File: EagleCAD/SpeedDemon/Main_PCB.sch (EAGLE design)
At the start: 71 parts, among them Q1 DMC2700, U3 LM3676, U4 STM32F072-LQFP48, X1 32.768kHz

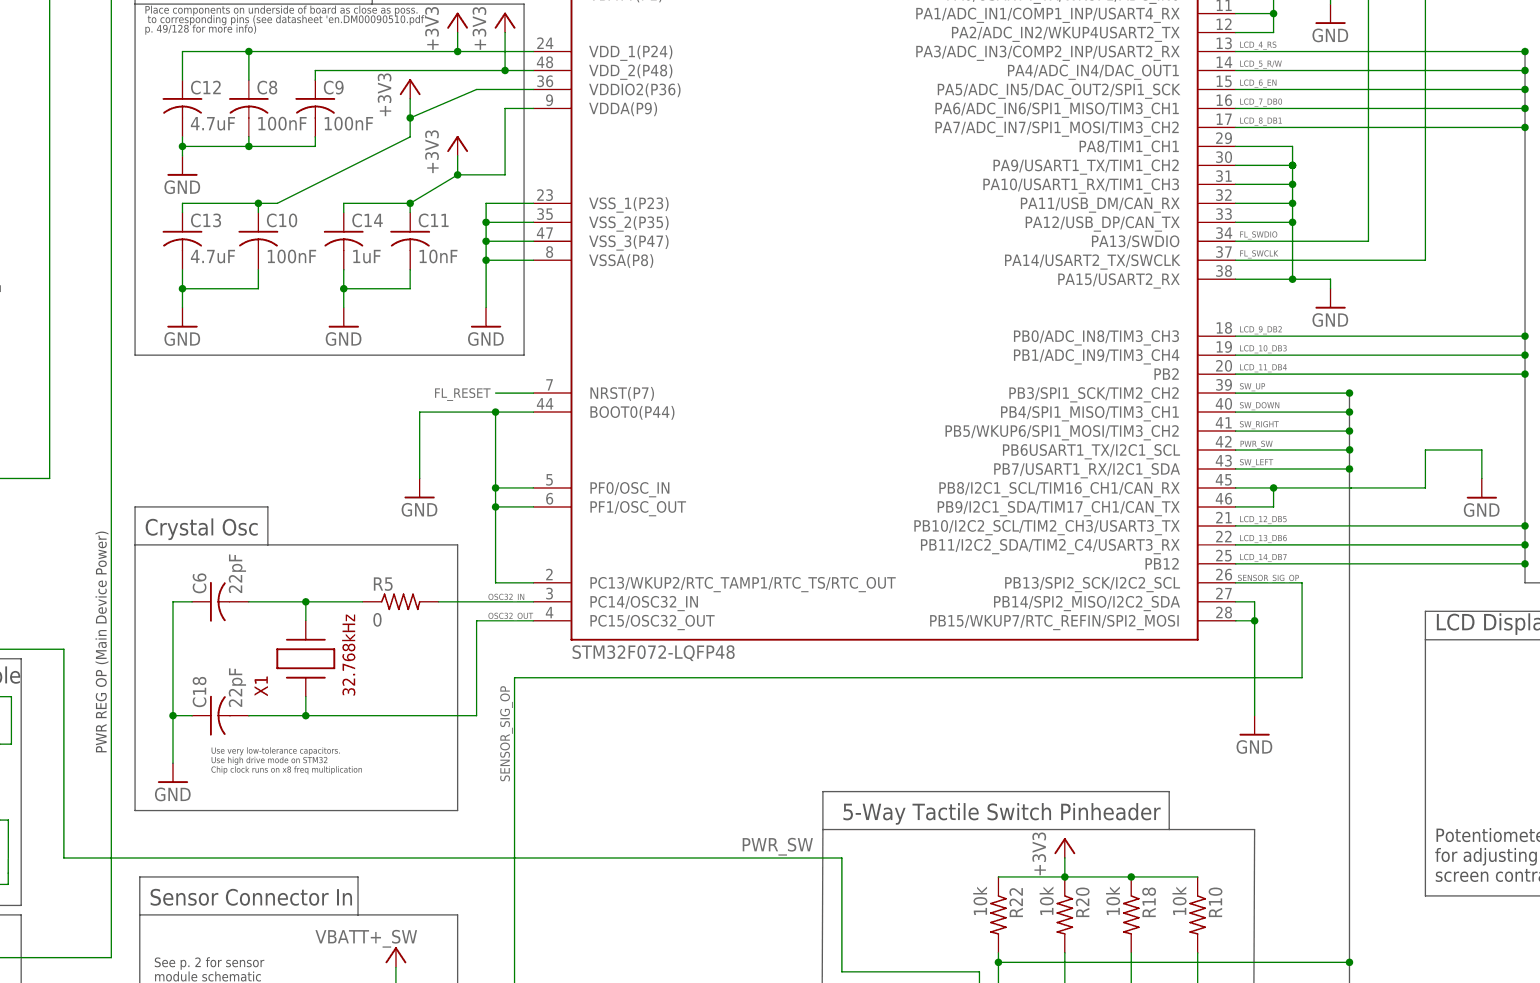
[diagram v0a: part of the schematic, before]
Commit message: added 8MHz oscillator citcuit to layout and schematic
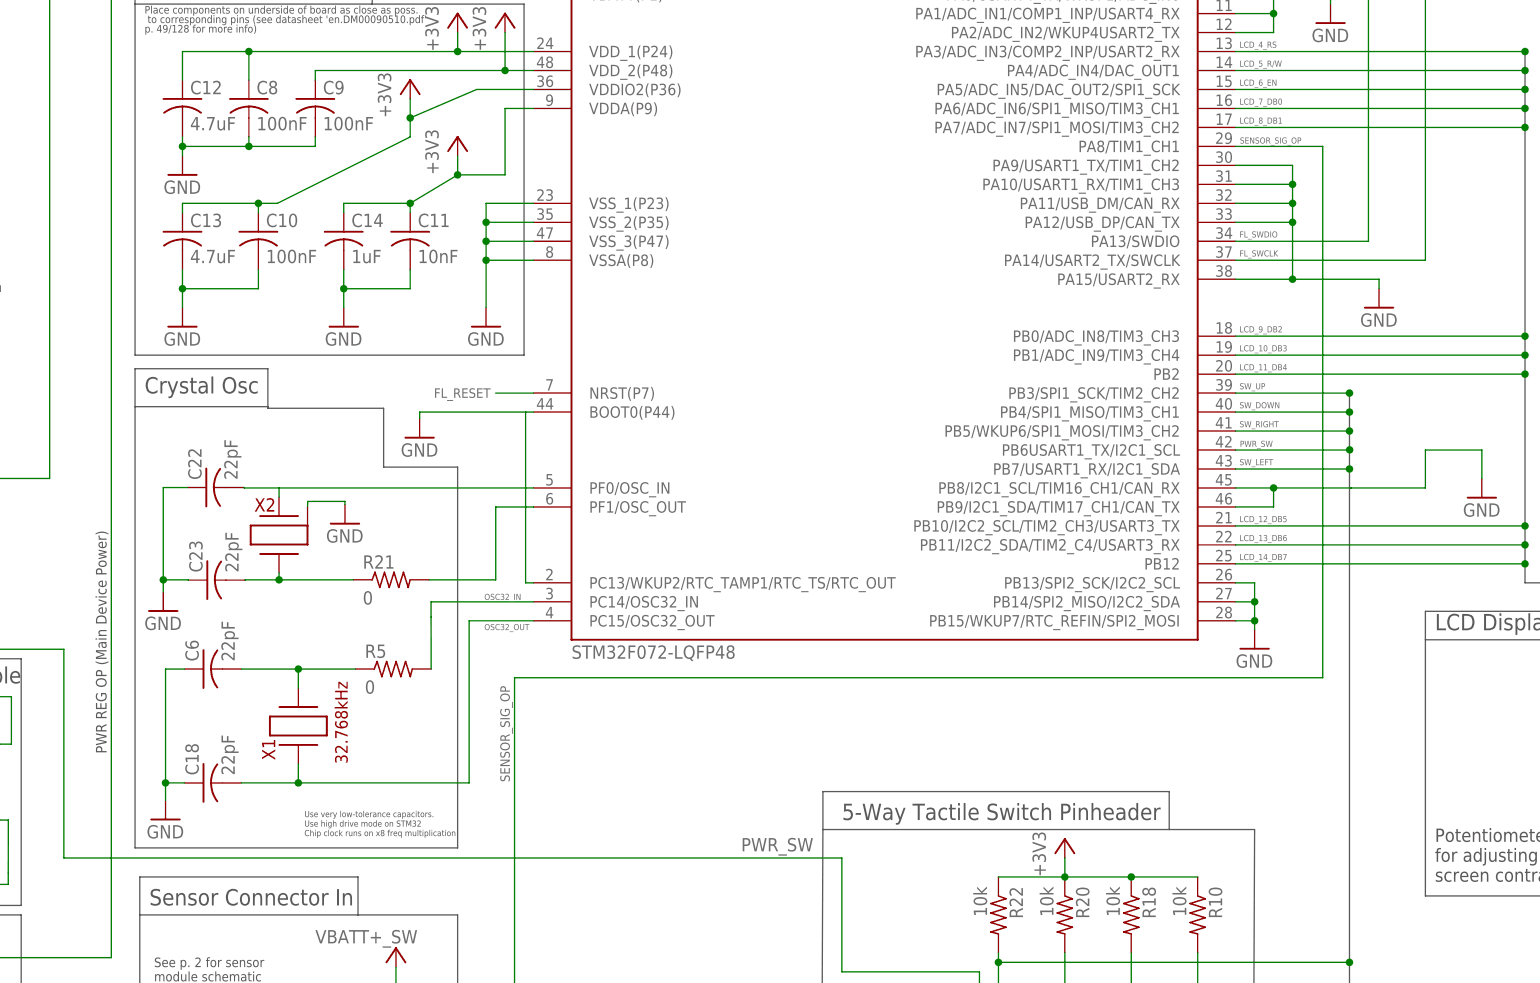
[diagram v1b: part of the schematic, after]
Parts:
- added C22, C23: 22pF, LCRD_SMD_generics:C_0805_NP
- added R21: 0, LCRD_SMD_generics:R_0805
- added X2: (no value), LCRD_SMD_generics:ABM3B-8.000MHZ-10-D-1-G-T
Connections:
- new net N$13: R21.2, U4.PF1/OSC_OUT
- new net N$17: C22.2, U4.PF0/OSC_IN, X2.1
- new net N$18: C23.2, R21.1, X2.2
- net GND: now also C22.1, C23.1, U4.PB13/SPI2_SCK/I2C2_SCL, X2.P$1; no longer U4.PA8/TIM1_CH1, U4.PF0/OSC_IN, U4.PF1/OSC_OUT
- net SENSOR_SIG_OP: now also U4.PA8/TIM1_CH1; no longer U4.PB13/SPI2_SCK/I2C2_SCL
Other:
- moved on the sheet: C18, C6, R5, X1

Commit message: schematic/layout detail work.
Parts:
- CONN1: device USB_jack_102-4008-1-ND:USB-MICRO-B -> USB_micro_jack:USB_JACK_102-4008-1-ND_USB-MICRO-B
- Q2: value (none) -> BSS138L
- U2: value (none) -> NC7S08M
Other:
- note removed: "BSS138LT1"
- moved on the sheet: C17, C22, C23, D3, D4, Q2, R2, R30

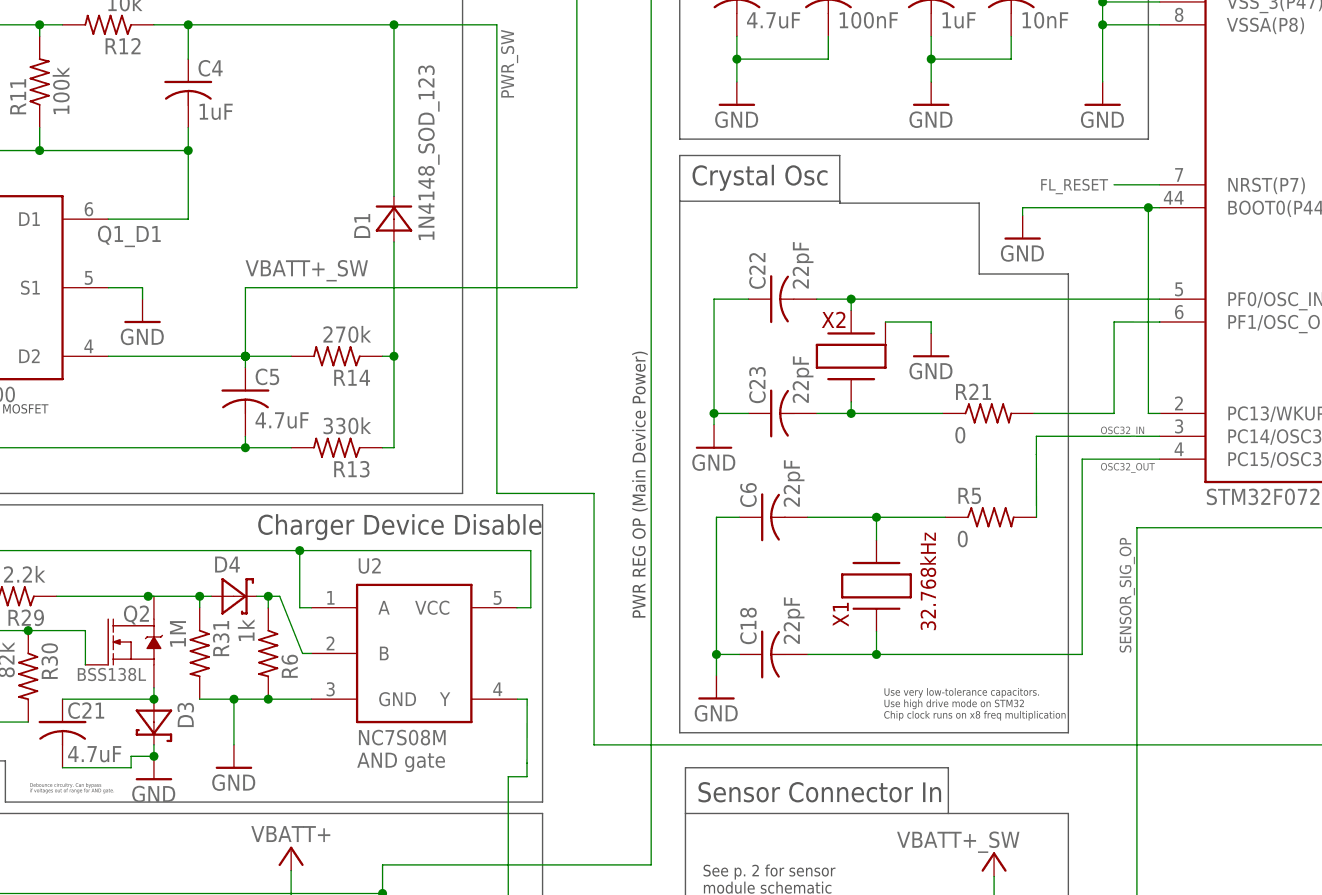
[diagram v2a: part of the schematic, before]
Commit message: final changes to power defeat logic
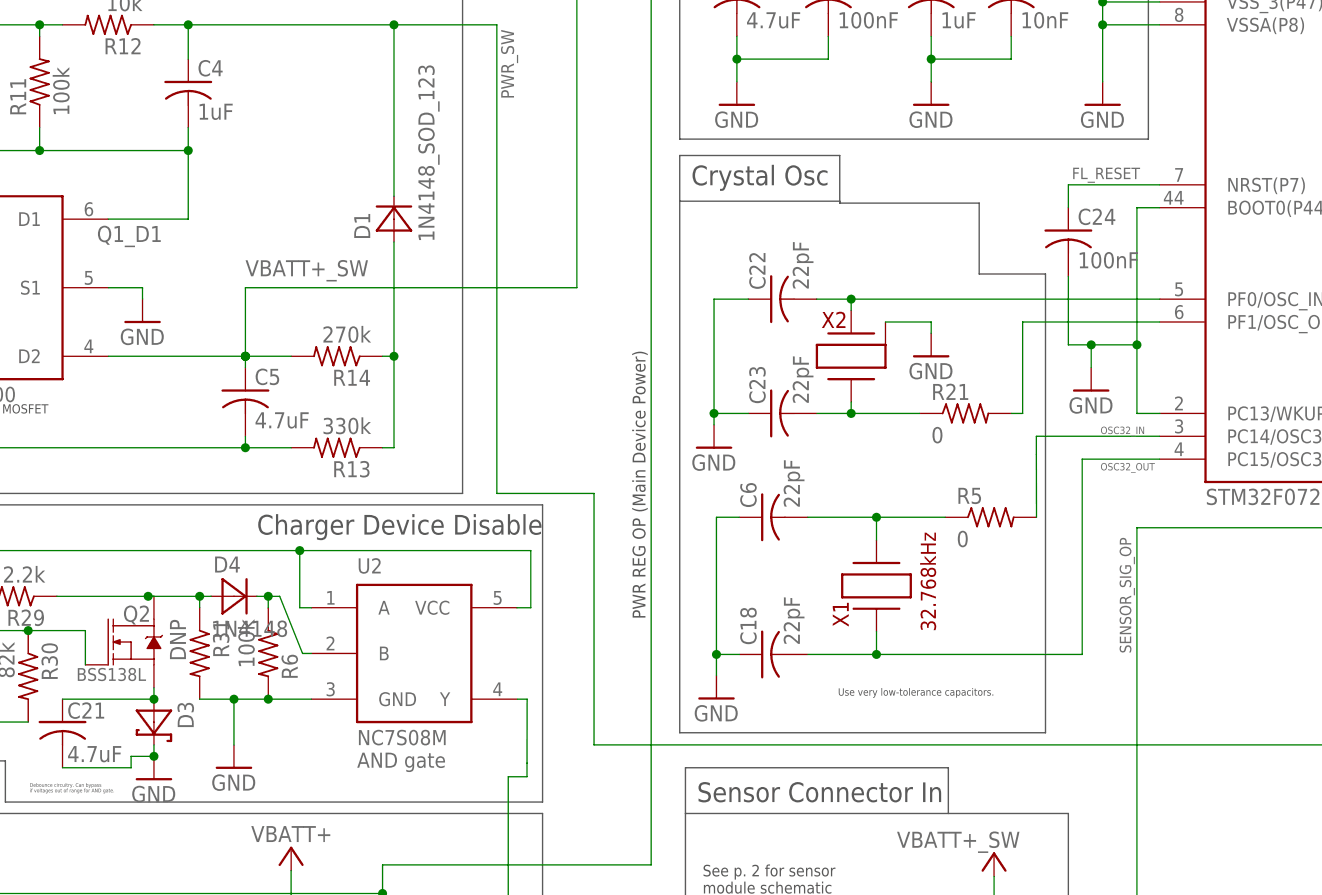
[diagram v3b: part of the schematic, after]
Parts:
- added C24: 100nF, 0805_generics:C_0805_NP
- D4: value (none) -> 1N4148; device LCRD_SMD_generics:CFSH05_SCHOTTKY -> LCRD_SMD_generics:1N4148_SOD_123
- R31: value 1M -> DNP
- R6: value 1k -> 100k
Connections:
- net FL_RESET: now also C24.1
- net GND: now also C24.2
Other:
- note removed: "Chip clock runs on x8 freq multiplication"
- note removed: "Use high drive mode on STM32"
- moved on the sheet: R21
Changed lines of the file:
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@@
 <setting verticaltext="up"/>
 </settings>
-<grid distance="0.05" unitdist="inch" unit="inch" style="lines" multiple="2" display="no" altdistance="0.01" altunitdist="inch" altunit="inch"/>
+<grid distance="0.1" unitdist="inch" unit="inch" style="lines" multiple="1" display="no" altdistance="0.01" altunitdist="inch" altunit="inch"/>
 <layers>
 <layer number="1" name="Top" color="4" fill="1" visible="no" active="no"/>
@@
 <part name="GND15" library="supply1" library_urn="urn:adsk.eagle:library:371" deviceset="GND" device=""/>
 <part name="R30" library="0805_generics" deviceset="R_0805" device="" value="82k"/>
-<part name="R31" library="0805_generics" deviceset="R_0805" device="" value="1M"/>
+<part name="R31" library="0805_generics" deviceset="R_0805" device="" value="DNP"/>
 <part name="U2" library="DMC2700" deviceset="NC7S08_SOT_23_5" device="" value="NC7S08M"/>
 <part name="VBATT_SW2" library="Custom_Power_Inlets" deviceset="VBATT+_SW" device=""/>
@@
 <part name="GND23" library="supply1" library_urn="urn:adsk.eagle:library:371" deviceset="GND" device=""/>
 <part name="GND28" library="supply1" library_urn="urn:adsk.eagle:library:371" deviceset="GND" device=""/>
-<part name="D4" library="LCRD_SMD_generics" deviceset="CFSH05_SCHOTTKY" device=""/>
-<part name="R6" library="0805_generics" deviceset="R_0805" device="" value="1k"/>
+<part name="R6" library="0805_generics" deviceset="R_0805" device="" value="100k"/>
 <part name="X2" library="LCRD_SMD_generics" deviceset="ABM3B-8.000MHZ-10-D-1-G-T" device=""/>
 <part name="R21" library="LCRD_SMD_generics" deviceset="R_0805" device="" value="0"/>
@@
 <part name="GND30" library="supply1" library_urn="urn:adsk.eagle:library:371" deviceset="GND" device=""/>
 <part name="CONN1" library="USB_micro_jack" deviceset="USB_JACK_102-4008-1-ND_USB-MICRO-B" device=""/>
+<part name="C24" library="0805_generics" deviceset="C_0805_NP" device="" value="100nF"/>
+<part name="D4" library="LCRD_SMD_generics" deviceset="1N4148_SOD_123" device="" value="1N4148"/>
 </parts>
 <sheets>
@@
 <text x="111.76" y="48.26" size="1.27" layer="97">See p. 2 for sensor
 module schematic</text>
-<wire x1="109.22" y1="66.12" x2="152.4" y2="66.12" width="0.1524" layer="97"/>
-<wire x1="152.4" y1="66.12" x2="152.4" y2="117.094" width="0.1524" layer="97"/>
-<wire x1="152.4" y1="117.094" x2="142.494" y2="117.094" width="0.1524" layer="97"/>
+<wire x1="109.22" y1="66.12" x2="149.86" y2="66.12" width="0.1524" layer="97"/>
+<wire x1="149.86" y1="66.12" x2="149.86" y2="117.094" width="0.1524" layer="97"/>
+<wire x1="149.86" y1="117.094" x2="142.494" y2="117.094" width="0.1524" layer="97"/>
 <wire x1="142.494" y1="117.094" x2="142.494" y2="124.968" width="0.1524" layer="97"/>
 <wire x1="142.494" y1="124.968" x2="127" y2="124.968" width="0.1524" layer="97"/>
@@
 UP
 GND</text>
-<text x="131.88" y="70.24" size="0.8128" layer="97">Use very low-tolerance capacitors.</text>
-<text x="131.88" y="68.97" size="0.8128" layer="97">Use high drive mode on STM32</text>
-<text x="131.88" y="67.7" size="0.8128" layer="97">Chip clock runs on x8 freq multiplication</text>
+<text x="126.8" y="70.24" size="0.8128" layer="97">Use very low-tolerance capacitors.</text>
 <text x="218.44" y="15.84" size="0.8128" layer="97" rot="R90">See p.2 for switch connections</text>
 <text x="26.035" y="180.34" size="1.778" layer="97">+</text>
@@
 <instance part="JP5" gate="A" x="117.475" y="41.91" rot="R180"/>
 <instance part="CN1" gate="G$1" x="19.05" y="179.705" rot="R180"/>
-<instance part="GND1" gate="1" x="147.32" y="121.03"/>
+<instance part="GND1" gate="1" x="154.94" y="104.14"/>
 <instance part="GND24" gate="1" x="269.24" y="176.53"/>
 <instance part="GND25" gate="1" x="275.74" y="138.43"/>
@@
 <instance part="GND23" gate="1" x="50.8" y="60.96"/>
 <instance part="GND28" gate="1" x="16.51" y="66.04"/>
-<instance part="D4" gate="G$1" x="59.69" y="81.28"/>
 <instance part="R6" gate="G$1" x="63.5" y="74.93" smashed="yes" rot="R270">
 <attribute name="NAME" x="64.9986" y="74.93" size="1.778" layer="95" rot="R270"/>
@@
 <attribute name="VALUE" x="134.874" y="102.87" size="1.6764" layer="94" rot="R90"/>
 </instance>
-<instance part="R21" gate="G$1" x="143.51" y="101.6"/>
+<instance part="R21" gate="G$1" x="140.97" y="101.6"/>
 <instance part="GND29" gate="1" x="137.16" y="107.95"/>
 <instance part="C22" gate="G$1" x="119.38" y="114.3" rot="R90"/>
@@
 <instance part="GND30" gate="1" x="113.03" y="97.79"/>
 <instance part="CONN1" gate="G$1" x="15.24" y="234.95"/>
+<instance part="C24" gate="G$1" x="152.4" y="121.92"/>
+<instance part="D4" gate="&gt;NAME" x="59.69" y="81.28" smashed="yes">
+<attribute name="NAME" x="57.3786" y="83.9216" size="1.778" layer="95"/>
+<attribute name="VALUE" x="57.1246" y="76.7842" size="1.778" layer="96"/>
+</instance>
 </instances>
 <busses>
@@
 <segment>
 <pinref part="U4" gate="G$1" pin="NRST(P7)"/>
-<wire x1="162.56" y1="127" x2="157.48" y2="127" width="0.1524" layer="91"/>
-<label x="149.225" y="126.365" size="1.27" layer="95"/>
+<wire x1="162.56" y1="127" x2="152.4" y2="127" width="0.1524" layer="91"/>
+<label x="152.781" y="127.635" size="1.27" layer="95"/>
+<pinref part="C24" gate="G$1" pin="1"/>
+<wire x1="152.4" y1="127" x2="152.4" y2="124.46" width="0.1524" layer="91"/>
 </segment>
 </net>
@@
 <wire x1="234.95" y1="27.27" x2="234.95" y2="32.35" width="0.1524" layer="91"/>
 <wire x1="234.95" y1="32.35" x2="241.3" y2="32.35" width="0.1524" layer="91"/>
-</segment>
-<segment>
-<pinref part="GND1" gate="1" pin="GND"/>
-<pinref part="U4" gate="G$1" pin="BOOT0(P44)"/>
-<wire x1="162.56" y1="124.46" x2="161.29" y2="124.46" width="0.1524" layer="91"/>
-<wire x1="161.29" y1="124.46" x2="147.32" y2="124.46" width="0.1524" layer="91"/>
-<wire x1="147.32" y1="124.46" x2="147.32" y2="123.57" width="0.1524" layer="91"/>
-<pinref part="U4" gate="G$1" pin="PC13/WKUP2/RTC_TAMP1/RTC_TS/RTC_OUT"/>
-<wire x1="161.29" y1="124.46" x2="161.29" y2="101.6" width="0.1524" layer="91"/>
-<wire x1="161.29" y1="101.6" x2="162.56" y2="101.6" width="0.1524" layer="91"/>
-<junction x="161.29" y="124.46"/>
 </segment>
 <segment>
@@
 <wire x1="50.8" y1="64.77" x2="50.8" y2="63.5" width="0.1524" layer="91"/>
 <junction x="50.8" y="63.5"/>
+</segment>
+<segment>
+<pinref part="C24" gate="G$1" pin="2"/>
+<pinref part="U4" gate="G$1" pin="BOOT0(P44)"/>
+<wire x1="152.4" y1="109.22" x2="152.4" y2="116.84" width="0.1524" layer="91"/>
+<wire x1="162.56" y1="124.46" x2="160.02" y2="124.46" width="0.1524" layer="91"/>
+<pinref part="U4" gate="G$1" pin="PC13/WKUP2/RTC_TAMP1/RTC_TS/RTC_OUT"/>
+<wire x1="160.02" y1="124.46" x2="160.02" y2="109.22" width="0.1524" layer="91"/>
+<wire x1="160.02" y1="109.22" x2="160.02" y2="101.6" width="0.1524" layer="91"/>
+<wire x1="160.02" y1="101.6" x2="162.56" y2="101.6" width="0.1524" layer="91"/>
+<wire x1="152.4" y1="109.22" x2="154.94" y2="109.22" width="0.1524" layer="91"/>
+<junction x="160.02" y="109.22"/>
+<pinref part="GND1" gate="1" pin="GND"/>
+<wire x1="154.94" y1="109.22" x2="160.02" y2="109.22" width="0.1524" layer="91"/>
+<wire x1="154.94" y1="109.22" x2="154.94" y2="106.68" width="0.1524" layer="91"/>
+<junction x="154.94" y="109.22"/>
 </segment>
 </net>
@@
 </segment>
 </net>
-<net name="N$13" class="0">
-<segment>
-<pinref part="R21" gate="G$1" pin="2"/>
-<wire x1="148.59" y1="101.6" x2="157.48" y2="101.6" width="0.1524" layer="91"/>
-<wire x1="157.48" y1="101.6" x2="157.48" y2="111.76" width="0.1524" layer="91"/>
-<pinref part="U4" gate="G$1" pin="PF1/OSC_OUT"/>
-<wire x1="157.48" y1="111.76" x2="162.56" y2="111.754" width="0.1524" layer="91"/>
-<wire x1="162.56" y1="111.754" x2="162.56" y2="111.76" width="0.1524" layer="91"/>
-</segment>
-</net>
 <net name="N$18" class="0">
 <segment>
 <pinref part="R21" gate="G$1" pin="1"/>
 <pinref part="X2" gate="G$1" pin="2"/>
-<wire x1="138.43" y1="101.6" x2="128.27" y2="101.6" width="0.1524" layer="91"/>
+<wire x1="135.89" y1="101.6" x2="128.27" y2="101.6" width="0.1524" layer="91"/>
 <wire x1="128.27" y1="101.6" x2="128.27" y2="102.87" width="0.1524" layer="91"/>
 <pinref part="C23" gate="G$1" pin="2"/>
@@
 <pinref part="R31" gate="G$1" pin="1"/>
 <wire x1="55.88" y1="81.28" x2="55.88" y2="80.01" width="0.1524" layer="91"/>
-<pinref part="D4" gate="G$1" pin="A"/>
 <wire x1="55.88" y1="81.28" x2="57.15" y2="81.28" width="0.1524" layer="91"/>
 <junction x="55.88" y="81.28"/>
+<pinref part="D4" gate="&gt;NAME" pin="A"/>
 </segment>
 </net>
 <net name="N$11" class="0">
 <segment>
-<pinref part="D4" gate="G$1" pin="C"/>
 <pinref part="R6" gate="G$1" pin="1"/>
 <wire x1="62.23" y1="81.28" x2="63.5" y2="81.28" width="0.1524" layer="91"/>
@@
 <pinref part="U2" gate="G$1" pin="B"/>
 <wire x1="67.31" y1="74.93" x2="68.29" y2="74.93" width="0.1524" layer="91"/>
+<pinref part="D4" gate="&gt;NAME" pin="C"/>
 </segment>
 </net>
@@
 </segment>
 </net>
+<net name="N$13" class="0">
+<segment>
+<pinref part="U4" gate="G$1" pin="PF1/OSC_OUT"/>
+<wire x1="162.56" y1="111.76" x2="147.32" y2="111.76" width="0.1524" layer="91"/>
+<wire x1="147.32" y1="111.76" x2="147.32" y2="101.6" width="0.1524" layer="91"/>
+<pinref part="R21" gate="G$1" pin="2"/>
+<wire x1="146.05" y1="101.6" x2="147.32" y2="101.6" width="0.1524" layer="91"/>
+</segment>
+</net>
